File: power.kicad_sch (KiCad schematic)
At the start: 7 parts, among them U9 LM7805_TO220

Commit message: Changes after tweaking
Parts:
- D15, D16: value 1N4001 -> 1N5818
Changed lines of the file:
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@@
     (in_bom yes) (on_board yes)
     (property "Reference" "D15" (id 0) (at 96.52 39.37 0))
-    (property "Value" "1N4001" (id 1) (at 96.52 36.83 0))
+    (property "Value" "1N5818" (id 1) (at 96.52 36.83 0))
     (property "Footprint" "Rumblesan_Footprints:Diode_THT_P7.62mm_Horizontal" (id 2) (at 96.52 33.02 0)
       (effects (font (size 1.27 1.27)) hide)
@@
     (in_bom yes) (on_board yes)
     (property "Reference" "D16" (id 0) (at 96.52 52.07 0))
-    (property "Value" "1N4001" (id 1) (at 96.52 49.53 0))
+    (property "Value" "1N5818" (id 1) (at 96.52 49.53 0))
     (property "Footprint" "Rumblesan_Footprints:Diode_THT_P7.62mm_Horizontal" (id 2) (at 96.52 45.72 0)
       (effects (font (size 1.27 1.27)) hide)

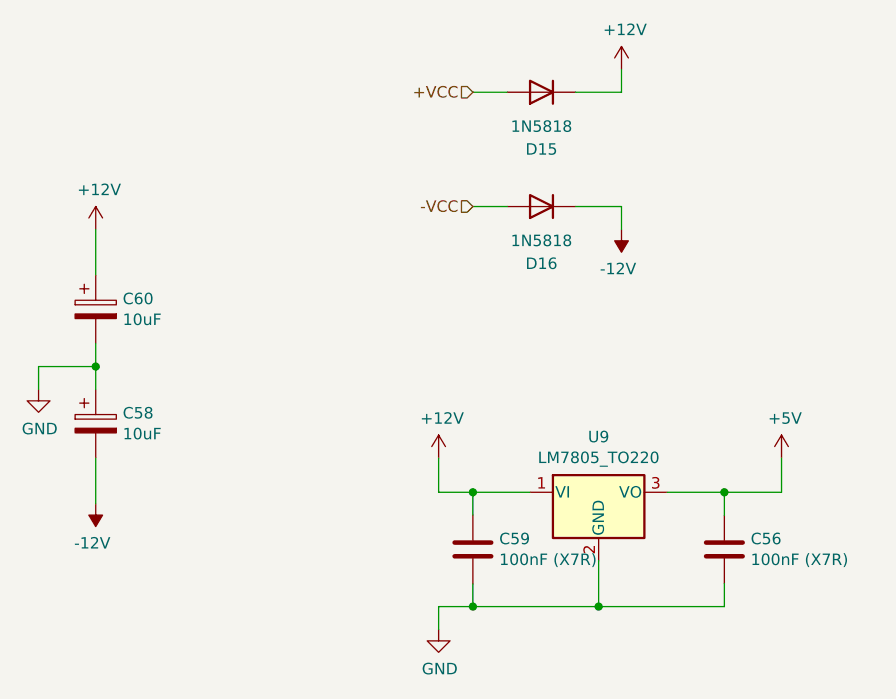
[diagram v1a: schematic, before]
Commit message: Tweaks and fixes for rev 4
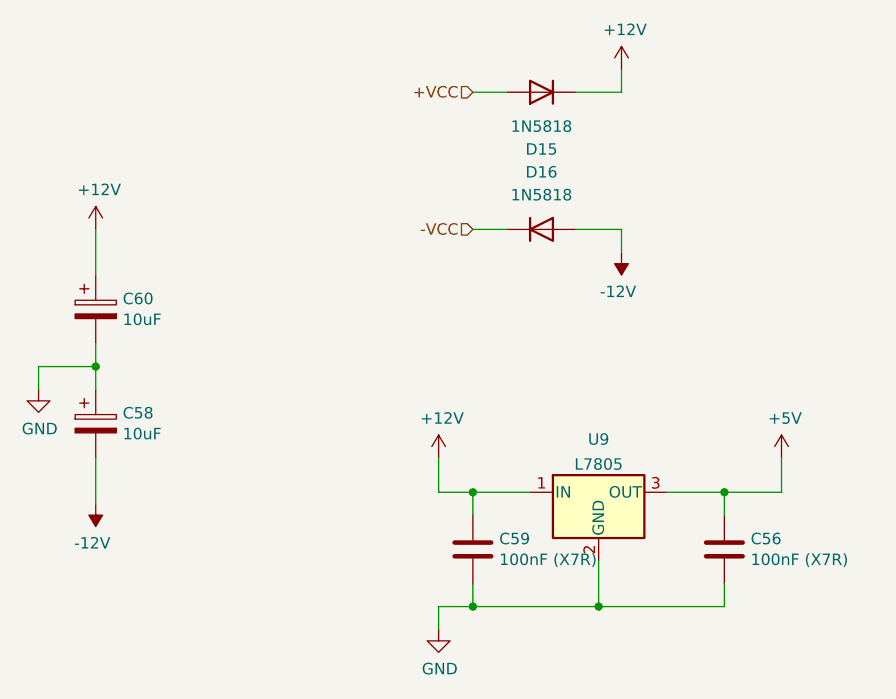
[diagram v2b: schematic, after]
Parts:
- removed U9: LM7805_TO220, Package_TO_SOT_THT:TO-220-3_Horizontal_TabDown, symbol Regulator_Linear:LM7805_TO220
- added U9: L7805, Package_TO_SOT_THT:TO-220-3_Horizontal_TabDown, symbol Regulator_Linear:L7805
- D15, D16: footprint Rumblesan_Footprints:Diode_THT_P7.62mm_Horizontal -> Diode_THT:D_A-405_P10.16mm_Horizontal
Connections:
- net +12V: now also U9.1 (IN)
- net +5V: now also U9.3 (OUT)
- net -12V: now also D16.2 (A); no longer D16.1 (K)
- net -VCC: now also D16.1 (K); no longer D16.2 (A)
- net GND: now also U9.2 (GND)
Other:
- moved on the sheet: D16
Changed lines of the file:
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@@
   (paper "A4")
   (title_block
-    (date "2022-01-13")
-    (rev "v03")
+    (date "2022-02-11")
+    (rev "v04")
     (comment 2 "creativecommons.org/licenses/by/4.0/")
     (comment 3 "License: CC BY 4.0")
@@
     (stroke (width 0) (type default) (color 0 0 0 0))
   )
-  (wire (pts (xy 88.9 45.72) (xy 92.71 45.72))
+  (wire (pts (xy 88.9 48.26) (xy 92.71 48.26))
     (stroke (width 0) (type default) (color 0 0 0 0))
   )
@@
     (stroke (width 0) (type default) (color 0 0 0 0))
   )
-  (wire (pts (xy 105.41 45.72) (xy 105.41 48.26))
-    (stroke (width 0) (type default) (color 0 0 0 0))
-  )
-  (wire (pts (xy 100.33 45.72) (xy 105.41 45.72))
+  (wire (pts (xy 105.41 48.26) (xy 105.41 50.8))
+    (stroke (width 0) (type default) (color 0 0 0 0))
+  )
+  (wire (pts (xy 100.33 48.26) (xy 105.41 48.26))
     (stroke (width 0) (type default) (color 0 0 0 0))
   )
@@
     (effects (font (size 1.27 1.27)) (justify right))
   )
-  (hierarchical_label "-VCC" (shape input) (at 88.9 45.72 180)
+  (hierarchical_label "-VCC" (shape input) (at 88.9 48.26 180)
     (effects (font (size 1.27 1.27)) (justify right))
-  )
-  (symbol (lib_id "Regulator_Linear:LM7805_TO220") (at 102.87 77.47 0) (unit 1)
-    (in_bom yes) (on_board yes)
-    (property "Reference" "U9" (id 0) (at 102.87 71.3232 0))
-    (property "Value" "LM7805_TO220" (id 1) (at 102.87 73.6346 0))
-    (property "Footprint" "Package_TO_SOT_THT:TO-220-3_Horizontal_TabDown" (id 2) (at 102.87 71.755 0)
-      (effects (font (size 1.27 1.27) italic) hide)
-    )
-    (property "Datasheet" "https://www.onsemi.cn/PowerSolutions/document/MC7800-D.PDF" (id 3) (at 102.87 78.74 0)
-      (effects (font (size 1.27 1.27)) hide)
-    )
-    (pin "1")
-    (pin "2")
-    (pin "3")
   )
   (symbol (lib_id "Device:C") (at 116.84 83.82 180) (unit 1)
@@
     (property "Reference" "D15" (id 0) (at 96.52 39.37 0))
     (property "Value" "1N5818" (id 1) (at 96.52 36.83 0))
-    (property "Footprint" "Rumblesan_Footprints:Diode_THT_P7.62mm_Horizontal" (id 2) (at 96.52 33.02 0)
+    (property "Footprint" "Diode_THT:D_A-405_P10.16mm_Horizontal" (id 2) (at 96.52 33.02 0)
       (effects (font (size 1.27 1.27)) hide)
     )
@@
     (pin "2")
   )
-  (symbol (lib_id "Device:D") (at 96.52 45.72 180) (unit 1)
-    (in_bom yes) (on_board yes)
-    (property "Reference" "D16" (id 0) (at 96.52 52.07 0))
-    (property "Value" "1N5818" (id 1) (at 96.52 49.53 0))
-    (property "Footprint" "Rumblesan_Footprints:Diode_THT_P7.62mm_Horizontal" (id 2) (at 96.52 45.72 0)
-      (effects (font (size 1.27 1.27)) hide)
-    )
-    (property "Datasheet" "~" (id 3) (at 96.52 45.72 0)
-      (effects (font (size 1.27 1.27)) hide)
-    )
-    (pin "1")
-    (pin "2")
+  (symbol (lib_id "Device:D") (at 96.52 48.26 0) (unit 1)
+    (in_bom yes) (on_board yes)
+    (property "Reference" "D16" (id 0) (at 96.52 41.91 0))
+    (property "Value" "1N5818" (id 1) (at 96.52 44.45 0))
+    (property "Footprint" "Diode_THT:D_A-405_P10.16mm_Horizontal" (id 2) (at 96.52 48.26 0)
+      (effects (font (size 1.27 1.27)) hide)
+    )
+    (property "Datasheet" "~" (id 3) (at 96.52 48.26 0)
+      (effects (font (size 1.27 1.27)) hide)
+    )
+    (pin "1")
+    (pin "2")
+  )
+  (symbol (lib_id "Regulator_Linear:L7805") (at 102.87 77.47 0) (unit 1)
+    (in_bom yes) (on_board yes) (fields_autoplaced)
+    (property "Reference" "U9" (id 0) (at 102.87 71.5985 0))
+    (property "Value" "L7805" (id 1) (at 102.87 74.3736 0))
+    (property "Footprint" "Package_TO_SOT_THT:TO-220-3_Horizontal_TabDown" (id 2) (at 103.505 81.28 0)
+      (effects (font (size 1.27 1.27) italic) (justify left) hide)
+    )
+    (property "Datasheet" "http://www.st.com/content/ccc/resource/technical/document/datasheet/41/4f/b3/b0/12/d4/47/88/CD00000444.pdf/files/CD00000444.pdf/jcr:content/translations/en.CD00000444.pdf" (id 3) (at 102.87 78.74 0)
+      (effects (font (size 1.27 1.27)) hide)
+    )
+    (pin "1")
+    (pin "2")
+    (pin "3")
   )
   (symbol (lib_id "power:GND") (at 40.64 66.04 0) (unit 1)
@@
     (pin "1")
   )
-  (symbol (lib_id "power:-12V") (at 105.41 48.26 180) (unit 1)
-    (in_bom yes) (on_board yes)
-    (property "Reference" "#PWR0176" (id 0) (at 105.41 50.8 0)
-      (effects (font (size 1.27 1.27)) hide)
-    )
-    (property "Value" "-12V" (id 1) (at 105.029 52.6542 0))
-    (property "Footprint" "" (id 2) (at 105.41 48.26 0)
-      (effects (font (size 1.27 1.27)) hide)
-    )
-    (property "Datasheet" "" (id 3) (at 105.41 48.26 0)
-      (effects (font (size 1.27 1.27)) hide)
-    )
+  (symbol (lib_id "power:-12V") (at 105.41 50.8 180) (unit 1)
+    (in_bom yes) (on_board yes)
+    (property "Reference" "#PWR0176" (id 0) (at 105.41 53.34 0)
+      (effects (font (size 1.27 1.27)) hide)
+    )
+    (property "Value" "-12V" (id 1) (at 105.029 55.1942 0))
+    (property "Footprint" "" (id 2) (at 105.41 50.8 0)
+      (effects (font (size 1.27 1.27)) hide)
+    )
+    (property "Datasheet" "" (id 3) (at 105.41 50.8 0)
+      (effects (font (size 1.27 1.27)) hide)
+    )
